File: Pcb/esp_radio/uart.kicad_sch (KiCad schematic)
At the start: 8 parts, among them J12 USB_B_Micro, U8 CH340E

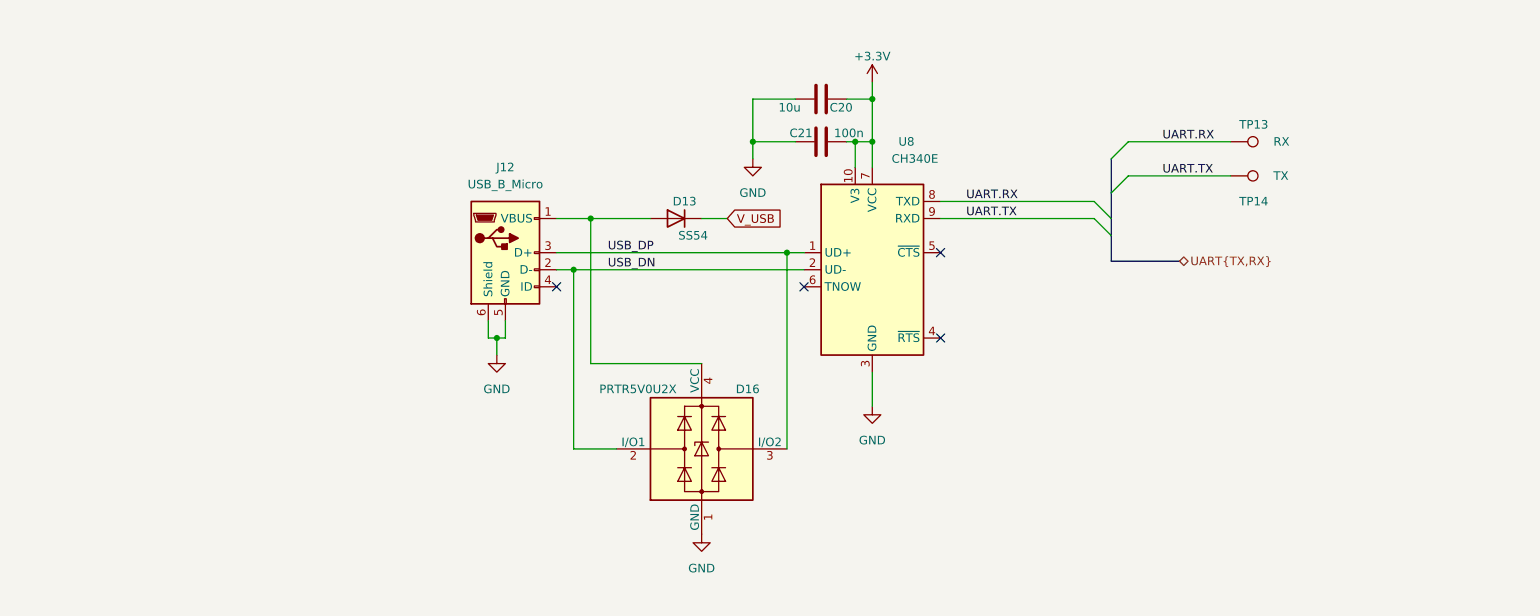
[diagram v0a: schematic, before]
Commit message: Move custom components to kicad_common_library.
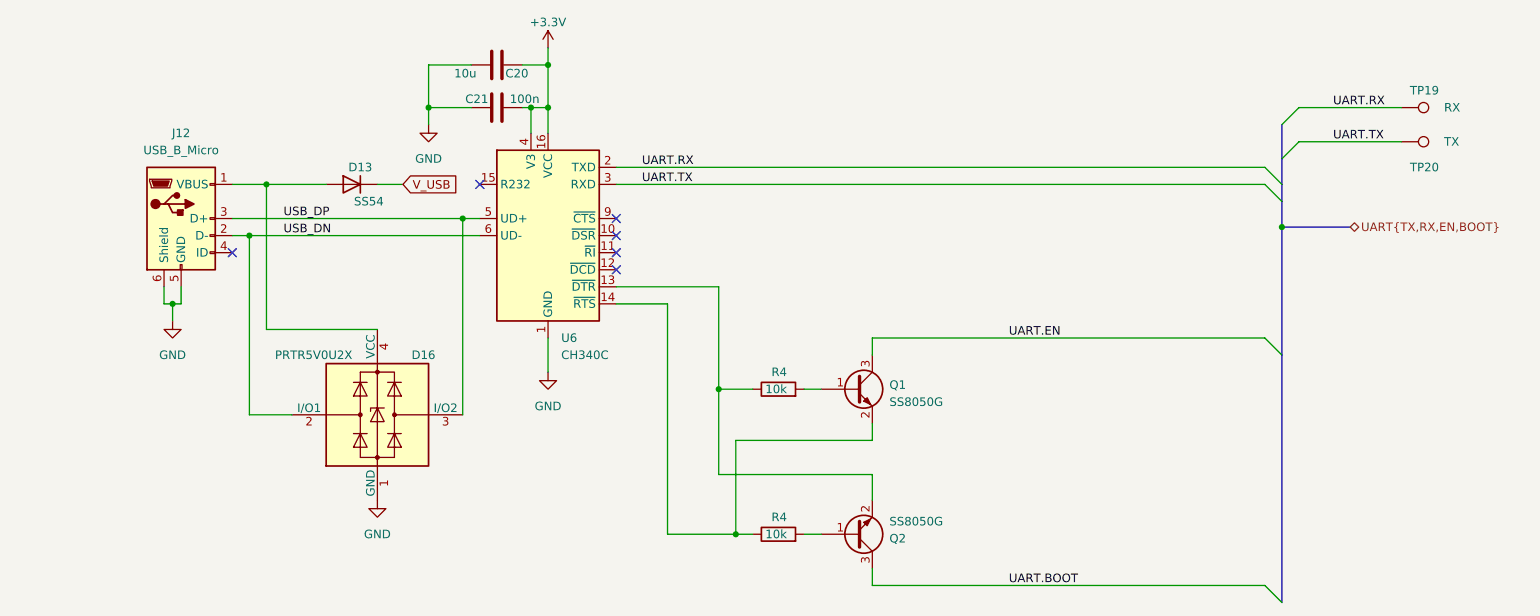
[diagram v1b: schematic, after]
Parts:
- removed U8: CH340E, Package_SO:MSOP-10_3x3mm_P0.5mm, symbol Interface_USB:CH340E
- added Q1, Q2: SS8050G, Package_TO_SOT_SMD:SOT-23, symbol kicad_common_lib:SS8050G
- added R4 (x2): 10k, symbol Device:R
- added U6: CH340C, Package_SO:SOIC-16_3.9x9.9mm_P1.27mm, symbol Interface_USB:CH340C
- renumbered TP13 to TP19, TP14 to TP20
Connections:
- net +3.3V: now also U6.16 (VCC), U6.4 (V3)
- net GND: now also U6.1 (GND)
- net UART.RX: now also U6.2 (TXD)
- net UART.TX: now also U6.3 (RXD)
- net USB_DN: now also U6.6 (UD-)
- net USB_DP: now also U6.5 (UD+)
- new net: Q1.2 (E), R4.1, U6.14 (~{RTS})
- new net: Q2.1 (B), R4.2
- new net: Q2.2 (E), R4.1, U6.13 (~{DTR})
- new net: Q1.1 (B), R4.2
- new net UART.BOOT: Q2.3 (C)
- new net UART.EN: Q1.3 (C)
- no-connect marks 4 -> 6
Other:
- moved on the sheet: C20, C21, D13, D16, J12, TP19, TP20

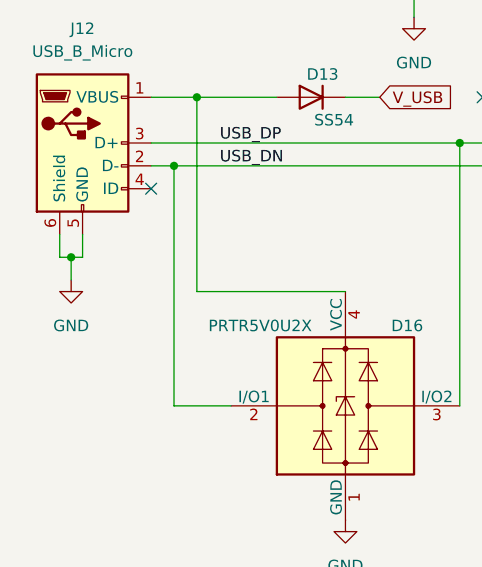
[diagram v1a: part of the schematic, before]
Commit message: Add components layout on PCB
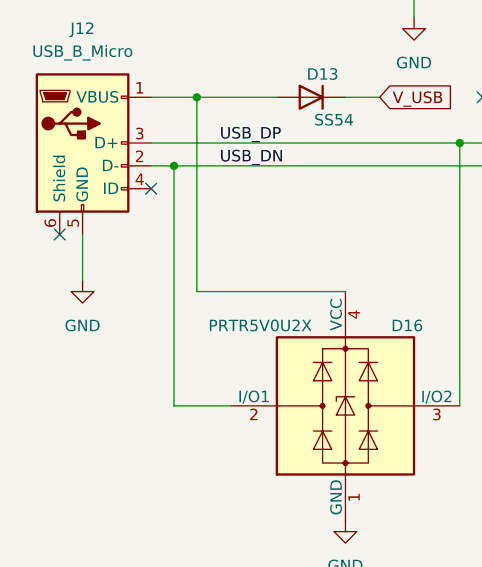
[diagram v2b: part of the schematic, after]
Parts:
- J12: footprint kicad_common_lib:USB_Micro-B_Amphenol_10104110_Horizontal -> Connector_PinHeader_2.54mm:PinHeader_1x05_P2.54mm_Vertical
- R4: footprint (none) -> kicad_common_lib:R_0805
- TP19, TP20: footprint (none) -> TestPoint:TestPoint_THTPad_D2.0mm_Drill1.0mm
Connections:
- net GND: no longer J12.6 (Shield)
- no-connect marks 6 -> 7
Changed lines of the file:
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@@
   (junction (at 121.92 66.04) (diameter 0.9144) (color 0 0 0 0)
   )
-  (junction (at 66.04 95.25) (diameter 0.9144) (color 0 0 0 0)
-  )
   (junction (at 149.86 129.54) (diameter 0) (color 0 0 0 0)
   )
@@
   )
   (no_connect (at 132.08 90.17))
+  (no_connect (at 64.77 92.71))
   (no_connect (at 74.93 87.63))
   (no_connect (at 132.08 85.09))
@@
     (stroke (width 0) (type default))
   )
-  (wire (pts (xy 64.77 95.25) (xy 66.04 95.25))
-    (stroke (width 0) (type solid))
-  )
   (wire (pts (xy 96.52 77.47) (xy 100.33 77.47))
     (stroke (width 0) (type solid))
@@
     (stroke (width 0) (type default))
   )
-  (wire (pts (xy 67.31 95.25) (xy 67.31 92.71))
+  (wire (pts (xy 67.31 92.71) (xy 67.31 97.79))
     (stroke (width 0) (type solid))
   )
@@
     (stroke (width 0) (type default))
   )
-  (wire (pts (xy 64.77 92.71) (xy 64.77 95.25))
-    (stroke (width 0) (type solid))
-  )
   (wire (pts (xy 147.32 107.95) (xy 152.4 107.95))
     (stroke (width 0) (type default))
@@
     (stroke (width 0) (type solid))
   )
-  (wire (pts (xy 66.04 95.25) (xy 67.31 95.25))
-    (stroke (width 0) (type solid))
-  )
   (wire (pts (xy 170.18 113.03) (xy 170.18 115.57))
     (stroke (width 0) (type default))
@@
   (wire (pts (xy 132.08 95.25) (xy 139.7 95.25))
     (stroke (width 0) (type default))
-  )
-  (wire (pts (xy 66.04 97.79) (xy 66.04 95.25))
-    (stroke (width 0) (type solid))
   )
   (bus (pts (xy 231.14 83.82) (xy 231.14 102.87))
@@
       (effects (font (size 1.27 1.27)) (justify left))
     )
-    (property "Footprint" "" (at 248.92 76.2 0)
+    (property "Footprint" "TestPoint:TestPoint_THTPad_D2.0mm_Drill1.0mm" (at 248.92 76.2 0)
       (effects (font (size 1.27 1.27)) hide)
     )
@@
       (effects (font (size 1.27 1.27)) (justify left))
     )
-    (property "Footprint" "" (at 156.21 131.318 90)
+    (property "Footprint" "kicad_common_lib:R_0805" (at 156.21 131.318 90)
       (effects (font (size 1.27 1.27)) hide)
     )
@@
       (effects (font (size 1.27 1.27)) (justify left))
     )
-    (property "Footprint" "" (at 156.21 109.728 90)
+    (property "Footprint" "kicad_common_lib:R_0805" (at 156.21 109.728 90)
       (effects (font (size 1.27 1.27)) hide)
     )
@@
     )
   )
-  (symbol (lib_id "power:GND") (at 66.04 97.79 0) (unit 1)
+  (symbol (lib_id "power:GND") (at 67.31 97.79 0) (unit 1)
     (in_bom yes) (on_board yes) (dnp no) (fields_autoplaced)
-    (property "Reference" "#PWR040" (at 66.04 104.14 0)
-      (effects (font (size 1.27 1.27)) hide)
-    )
-    (property "Value" "GND" (at 66.04 102.87 0)
-      (effects (font (size 1.27 1.27)))
-    )
-    (property "Footprint" "" (at 66.04 97.79 0)
-      (effects (font (size 1.27 1.27)) hide)
-    )
-    (property "Datasheet" "" (at 66.04 97.79 0)
+    (property "Reference" "#PWR040" (at 67.31 104.14 0)
+      (effects (font (size 1.27 1.27)) hide)
+    )
+    (property "Value" "GND" (at 67.31 102.87 0)
+      (effects (font (size 1.27 1.27)))
+    )
+    (property "Footprint" "" (at 67.31 97.79 0)
+      (effects (font (size 1.27 1.27)) hide)
+    )
+    (property "Datasheet" "" (at 67.31 97.79 0)
       (effects (font (size 1.27 1.27)) hide)
     )
@@
       (effects (font (size 1.27 1.27)) (justify left))
     )
-    (property "Footprint" "" (at 248.92 71.12 0)
+    (property "Footprint" "TestPoint:TestPoint_THTPad_D2.0mm_Drill1.0mm" (at 248.92 71.12 0)
       (effects (font (size 1.27 1.27)) hide)
     )
@@
       (effects (font (size 1.27 1.27)))
     )
-    (property "Footprint" "kicad_common_lib:USB_Micro-B_Amphenol_10104110_Horizontal" (at 71.12 83.82 0)
-      (effects (font (size 1.27 1.27)) hide)
-    )
+    (property "Footprint" "Connector_PinHeader_2.54mm:PinHeader_1x05_P2.54mm_Vertical" (at 71.12 83.82 0)
+      (effects (font (size 1.27 1.27)) hide)
+    )

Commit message: Finish board routing
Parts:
- added JP1: SolderJumper_2_Bridged, Jumper:SolderJumper-2_P1.3mm_Bridged_RoundedPad1.0x1.5mm, symbol Jumper:SolderJumper_2_Bridged
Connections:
- net GND: now also JP1.1 (A)
- net at J12.4 (ID): now also JP1.2 (B)
- no-connect marks 7 -> 6
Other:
- moved on the sheet: J12
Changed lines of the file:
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@@
   )
   (no_connect (at 132.08 90.17))
-  (no_connect (at 64.77 92.71))
-  (no_connect (at 74.93 87.63))
+  (no_connect (at 46.99 92.71))
   (no_connect (at 132.08 85.09))
   (no_connect (at 111.76 77.47))
@@
     (stroke (width 0) (type solid))
   )
+  (wire (pts (xy 57.15 87.63) (xy 60.96 87.63))
+    (stroke (width 0) (type default))
+  )
   (wire (pts (xy 119.38 66.04) (xy 121.92 66.04))
     (stroke (width 0) (type solid))
@@
     (stroke (width 0) (type default))
   )
-  (wire (pts (xy 74.93 85.09) (xy 77.47 85.09))
+  (wire (pts (xy 57.15 85.09) (xy 77.47 85.09))
     (stroke (width 0) (type solid))
   )
@@
     (stroke (width 0) (type default))
   )
+  (wire (pts (xy 60.96 95.25) (xy 60.96 97.79))
+    (stroke (width 0) (type default))
+  )
   (wire (pts (xy 118.11 59.69) (xy 121.92 59.69))
     (stroke (width 0) (type solid))
@@
     (stroke (width 0) (type default))
   )
+  (wire (pts (xy 77.47 85.09) (xy 77.47 111.76))
+    (stroke (width 0) (type solid))
+  )
   (wire (pts (xy 96.52 77.47) (xy 100.33 77.47))
     (stroke (width 0) (type solid))
@@
     (stroke (width 0) (type default))
   )
-  (wire (pts (xy 67.31 92.71) (xy 67.31 97.79))
+  (wire (pts (xy 49.53 92.71) (xy 49.53 97.79))
     (stroke (width 0) (type solid))
   )
@@
     (stroke (width 0) (type default))
   )
-  (wire (pts (xy 74.93 77.47) (xy 80.01 77.47))
+  (wire (pts (xy 57.15 77.47) (xy 80.01 77.47))
     (stroke (width 0) (type solid))
   )
@@
     (stroke (width 0) (type default))
   )
-  (wire (pts (xy 77.47 85.09) (xy 77.47 111.76))
-    (stroke (width 0) (type solid))
-  )
   (wire (pts (xy 96.52 99.06) (xy 80.01 99.06))
     (stroke (width 0) (type solid))
@@
     (stroke (width 0) (type solid))
   )
-  (wire (pts (xy 74.93 82.55) (xy 109.22 82.55))
+  (wire (pts (xy 57.15 82.55) (xy 109.22 82.55))
     (stroke (width 0) (type solid))
   )
@@
     )
   )
-  (symbol (lib_id "power:GND") (at 67.31 97.79 0) (unit 1)
-    (in_bom yes) (on_board yes) (dnp no) (fields_autoplaced)
-    (property "Reference" "#PWR040" (at 67.31 104.14 0)
-      (effects (font (size 1.27 1.27)) hide)
-    )
-    (property "Value" "GND" (at 67.31 102.87 0)
-      (effects (font (size 1.27 1.27)))
-    )
-    (property "Footprint" "" (at 67.31 97.79 0)
-      (effects (font (size 1.27 1.27)) hide)
-    )
-    (property "Datasheet" "" (at 67.31 97.79 0)
+  (symbol (lib_id "power:GND") (at 60.96 97.79 0) (unit 1)
+    (in_bom yes) (on_board yes) (dnp no) (fields_autoplaced)
+    (property "Reference" "#PWR072" (at 60.96 104.14 0)
+      (effects (font (size 1.27 1.27)) hide)
+    )
+    (property "Value" "GND" (at 60.96 102.87 0)
+      (effects (font (size 1.27 1.27)))
+    )
+    (property "Footprint" "" (at 60.96 97.79 0)
+      (effects (font (size 1.27 1.27)) hide)
+    )
+    (property "Datasheet" "" (at 60.96 97.79 0)
+      (effects (font (size 1.27 1.27)) hide)
+    )
+    (pin "1")
+    (instances
+      (project "esp_radio"
+        (path "/c9e2e0d2-0655-4f5e-8e13-71b41b1f7cfe/9103cc11-86bf-4fa8-956b-660d9ba42360"
+          (reference "#PWR072") (unit 1)
+        )
+      )
+    )
+  )
+  (symbol (lib_id "power:GND") (at 49.53 97.79 0) (unit 1)
+    (in_bom yes) (on_board yes) (dnp no) (fields_autoplaced)
+    (property "Reference" "#PWR040" (at 49.53 104.14 0)
+      (effects (font (size 1.27 1.27)) hide)
+    )
+    (property "Value" "GND" (at 49.53 102.87 0)
+      (effects (font (size 1.27 1.27)))
+    )
+    (property "Footprint" "" (at 49.53 97.79 0)
+      (effects (font (size 1.27 1.27)) hide)
+    )
+    (property "Datasheet" "" (at 49.53 97.79 0)
       (effects (font (size 1.27 1.27)) hide)
     )
@@
     )
   )
-  (symbol (lib_id "Connector:USB_B_Micro") (at 67.31 82.55 0) (unit 1)
-    (in_bom yes) (on_board yes) (dnp no)
-    (property "Reference" "J12" (at 67.31 69.85 0)
-      (effects (font (size 1.27 1.27)))
-    )
-    (property "Value" "USB_B_Micro" (at 67.31 72.39 0)
-      (effects (font (size 1.27 1.27)))
-    )
-    (property "Footprint" "Connector_PinHeader_2.54mm:PinHeader_1x05_P2.54mm_Vertical" (at 71.12 83.82 0)
-      (effects (font (size 1.27 1.27)) hide)
-    )
-    (property "Datasheet" "~" (at 71.12 83.82 0)
-      (effects (font (size 1.27 1.27)) hide)
-    )
+  (symbol (lib_id "Jumper:SolderJumper_2_Bridged") (at 60.96 91.44 90) (unit 1)
+    (in_bom yes) (on_board yes) (dnp no) (fields_autoplaced)
+    (property "Reference" "JP1" (at 63.5 92.075 90)
+      (effects (font (size 1.27 1.27)) (justify right))
+    )
+    (property "Value" "SolderJumper_2_Bridged" (at 58.42 91.44 0)
+      (effects (font (size 1.27 1.27)) hide)
+    )
+    (property "Footprint" "Jumper:SolderJumper-2_P1.3mm_Bridged_RoundedPad1.0x1.5mm" (at 60.96 91.44 0)
+      (effects (font (size 1.27 1.27)) hide)
+    )
+    (property "Datasheet" "~" (at 60.96 91.44 0)
+      (effects (font (size 1.27 1.27)) hide)
+    )
+    (pin "1")
+    (pin "2")
+    (instances
+      (project "esp_radio"
+        (path "/c9e2e0d2-0655-4f5e-8e13-71b41b1f7cfe/9686c251-96de-4991-9702-894d5bd1468a"
+          (reference "JP1") (unit 1)
+        )
+        (path "/c9e2e0d2-0655-4f5e-8e13-71b41b1f7cfe/9103cc11-86bf-4fa8-956b-660d9ba42360"
+          (reference "JP5") (unit 1)
+        )
+      )
+    )
+  )
+  (symbol (lib_id "Connector:USB_B_Micro") (at 49.53 82.55 0) (unit 1)
+    (in_bom yes) (on_board yes) (dnp no)
+    (property "Reference" "J12" (at 49.53 69.85 0)
+      (effects (font (size 1.27 1.27)))
+    )
+    (property "Value" "USB_B_Micro" (at 49.53 72.39 0)
+      (effects (font (size 1.27 1.27)))
+    )
+    (property "Footprint" "Connector_PinHeader_2.54mm:PinHeader_1x05_P2.54mm_Vertical" (at 53.34 83.82 0)
+      (effects (font (size 1.27 1.27)) hide)
+    )
+    (property "Datasheet" "~" (at 53.34 83.82 0)
+      (effects (font (size 1.27 1.27)) hide)
+    )
